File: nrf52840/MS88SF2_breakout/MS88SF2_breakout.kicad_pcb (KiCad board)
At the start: 2 copper layers, 25.6 x 36 mm, 4 parts, among them J1 Conn_01x14_Male, J2 Conn_01x14_Male, U1 MS88SF2

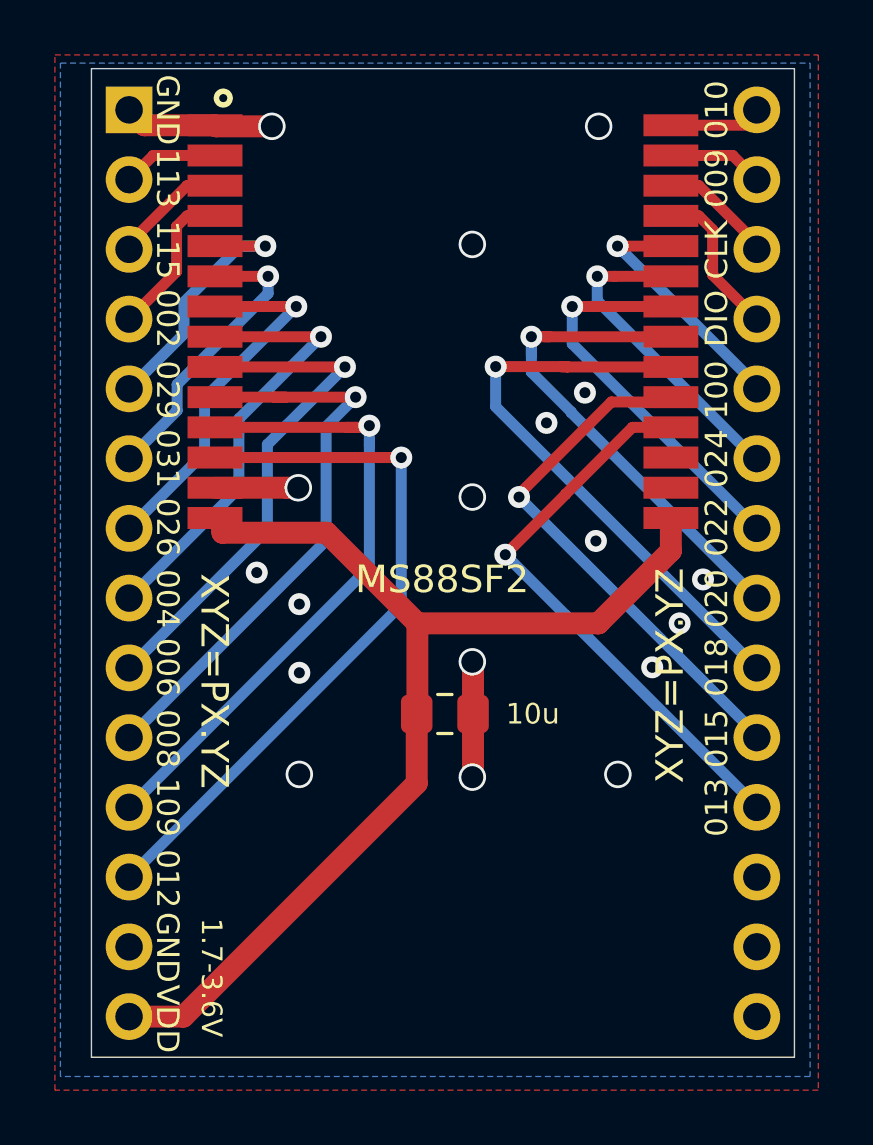
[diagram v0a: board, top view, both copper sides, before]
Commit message: nrf5: Add more gnd vias
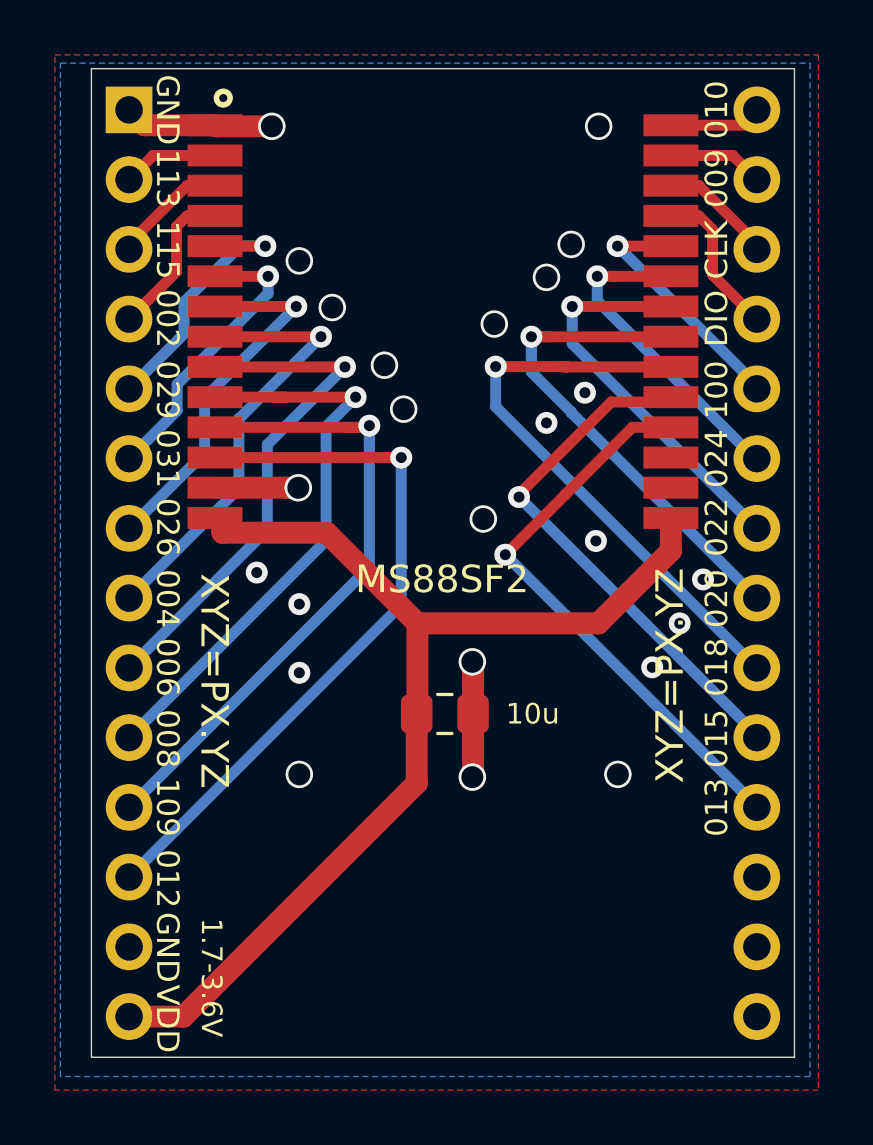
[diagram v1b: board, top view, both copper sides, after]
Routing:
- net GND: vias 18 -> 24
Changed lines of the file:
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@@
     (thickness 1.6)
     (drawings 37)
-    (tracks 162)
+    (tracks 168)
     (zones 0)
     (modules 4)
@@
   (via (at 69.162 73.762) (size 1) (drill 0.8) (layers F.Cu B.Cu) (net 2))
   (via (at 69.2 84.2) (size 1) (drill 0.8) (layers F.Cu B.Cu) (net 2))
-  (via (at 75.5 64.9) (size 1) (drill 0.8) (layers F.Cu B.Cu) (net 2))
+  (via (at 69.2 65.5) (size 1) (drill 0.8) (layers F.Cu B.Cu) (net 2))
   (via (at 68.2 60.6) (size 1) (drill 0.8) (layers F.Cu B.Cu) (net 2))
   (segment (start 63.562 60.562) (end 63 60) (width 0.8) (layer F.Cu) (net 2) (status 30))
   (segment (start 66.13 60.562) (end 63.562 60.562) (width 0.8) (layer F.Cu) (net 2) (status 30))
-  (via (at 75.5 74.1) (size 1) (drill 0.8) (layers F.Cu B.Cu) (net 2))
+  (via (at 75.9 74.9) (size 1) (drill 0.8) (layers F.Cu B.Cu) (net 2))
   (via (at 82.05 80.3) (size 0.8) (drill 0.4) (layers F.Cu B.Cu) (net 2))
   (via (at 83.05 78.7) (size 0.8) (drill 0.4) (layers F.Cu B.Cu) (net 2))
@@
   (via (at 80 75.7) (size 0.8) (drill 0.4) (layers F.Cu B.Cu) (net 2))
   (via (at 80.1 60.6) (size 1) (drill 0.8) (layers F.Cu B.Cu) (net 2))
+  (via (at 70.4 67.2) (size 1) (drill 0.8) (layers F.Cu B.Cu) (net 2))
+  (via (at 72.3 69.3) (size 1) (drill 0.8) (layers F.Cu B.Cu) (net 2))
+  (via (at 79.1 64.9) (size 1) (drill 0.8) (layers F.Cu B.Cu) (net 2))
+  (via (at 78.2 66.1) (size 1) (drill 0.8) (layers F.Cu B.Cu) (net 2))
+  (via (at 76.3 67.8) (size 1) (drill 0.8) (layers F.Cu B.Cu) (net 2))
+  (via (at 73 70.9) (size 1) (drill 0.8) (layers F.Cu B.Cu) (net 2))
   (segment (start 82.73 60.562) (end 83.438 60.562) (width 0.4) (layer F.Cu) (net 3) (status 30))
   (segment (start 85.69801 60.562) (end 85.86 60.40001) (width 0.4) (layer F.Cu) (net 3) (status 30))

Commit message: nrf5: Add bat holder
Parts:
- added BT1: Battery_Cell, !myfoots:CR2032_holder, F.Cu at (74.5, 83.5)
- moved C1 6.00 mm to (74.5, 88.0), turned to 180 degrees
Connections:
- J2 pad 15: (no net) -> Net-(J2-Pad15)
- J2 pad 16: (no net) -> Net-(J2-Pad16)
- J2 pad 17: (no net) -> Net-(J2-Pad17)
- U1 pad 16: (no net) -> Net-(U1-Pad16)
- U1 pad 17: (no net) -> Net-(U1-Pad17)
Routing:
- net +3V3: track 40.5 -> 50.7 mm
- net GND: track 12.7 -> 19.2 mm, vias 24 -> 22
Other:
- board text added: "+"
- board text added: "-"
